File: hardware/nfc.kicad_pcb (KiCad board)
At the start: 2 copper layers, 85 x 50 mm, 61 parts, among them J1 CONN_01X03, P1 CON-SENSOR2, P2 BOOT, P3 DEBUG, U1 XMC130024, U2 PN7150, U3 DRILL, U4 DRILL, U5 DRILL, U6 DRILL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

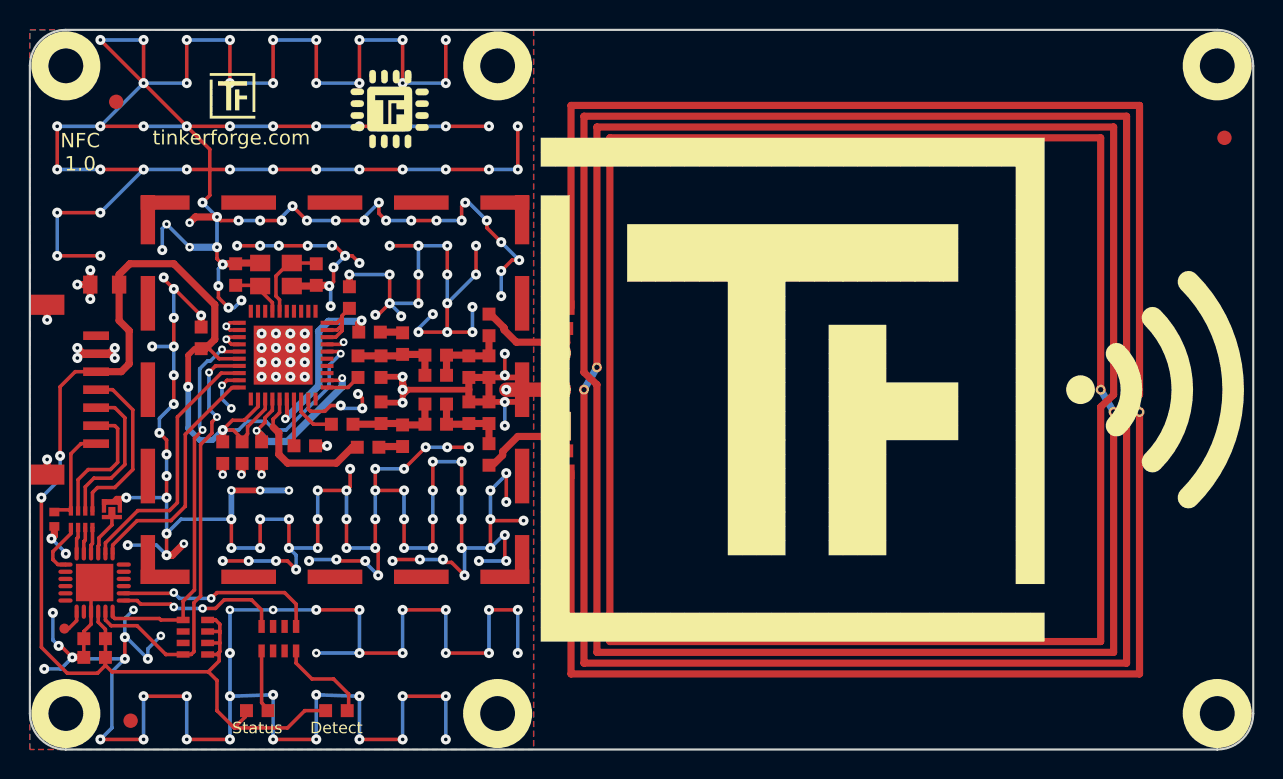
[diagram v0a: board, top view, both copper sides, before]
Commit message: add nfc 1.1
change board dimensions
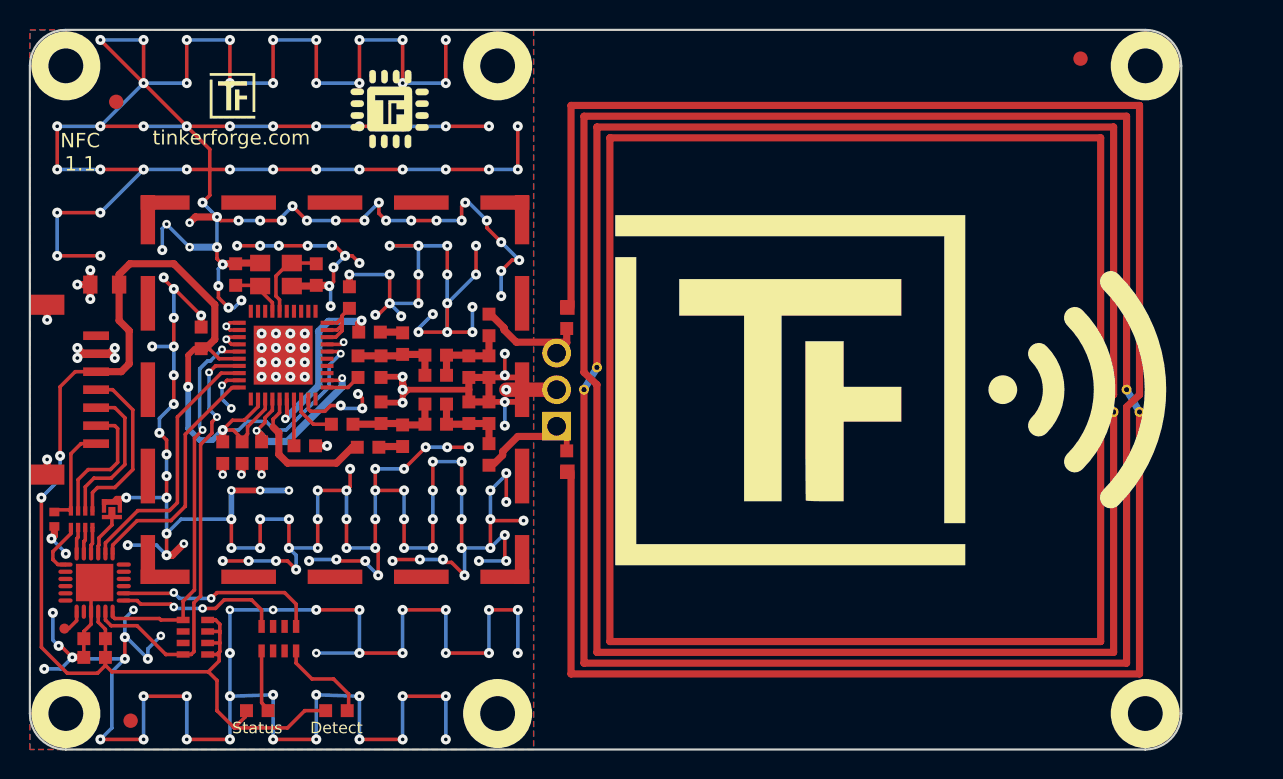
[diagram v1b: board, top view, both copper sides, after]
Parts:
- removed TF_ICON_35: , kicad-libraries:TF_ICON_35
- removed TF_ICON_35_FLIP: Val**, kicad-libraries:TF_ICON_35_FLIP
- added ?: , , B.Cu at (178.0, 77.0)
- added ?: , , F.Cu at (178.0, 77.0)
- added G***: LOGO, kicad-libraries:Logo_25x25, B.Cu at (163.3, 77.0)
- added G***: LOGO, kicad-libraries:Logo_25x25, F.Cu at (163.2, 77.0)
- moved Fiducial_Mark 11.4 mm to (183.4, 54.0)
- moved U3 5.00 mm to (187.9, 99.5)
- moved U4 5.00 mm to (187.9, 54.5)
- turned VAL to 180 degrees (x2)
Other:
- board size 85 x 50 mm -> 80 x 50 mm
- board text added: "NFC 1.1"
- board text removed: "NFC 1.0"

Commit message: fix settings
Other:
- rule pad_to_mask_clearance: 0.2 -> 0
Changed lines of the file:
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@@
     (pad_size 0.28956 0.89916)
     (pad_drill 0)
-    (pad_to_mask_clearance 0.2)
-    (solder_mask_min_width 0.25)
+    (pad_to_mask_clearance 0)
     (aux_axis_origin 110.4 52)
     (grid_origin 110.4 52)
     (visible_elements FFFFFF7F)
     (pcbplotparams
-      (layerselection 0x00000_00000001)
-      (usegerberextensions false)
+      (layerselection 0x010fc_ffffffff)
+      (usegerberextensions true)
       (usegerberattributes false)
       (usegerberadvancedattributes false)
@@
       (psnegative false)
       (psa4output false)
-      (plotreference true)
-      (plotvalue true)
+      (plotreference false)
+      (plotvalue false)
       (plotinvisibletext false)
       (padsonsilk false)
-      (subtractmaskfromsilk false)
+      (subtractmaskfromsilk true)
       (outputformat 1)
       (mirror false)
       (drillshape 0)
       (scaleselection 1)
-      (outputdirectory "prod/"))
+      (outputdirectory "pcb"))
   )
   (net 0 "")
